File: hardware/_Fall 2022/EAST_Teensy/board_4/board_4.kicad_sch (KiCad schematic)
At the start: 7 parts, among them J1 Conn_01x04, J2 Conn_02x09_Odd_Even, U1 Teensy4.1

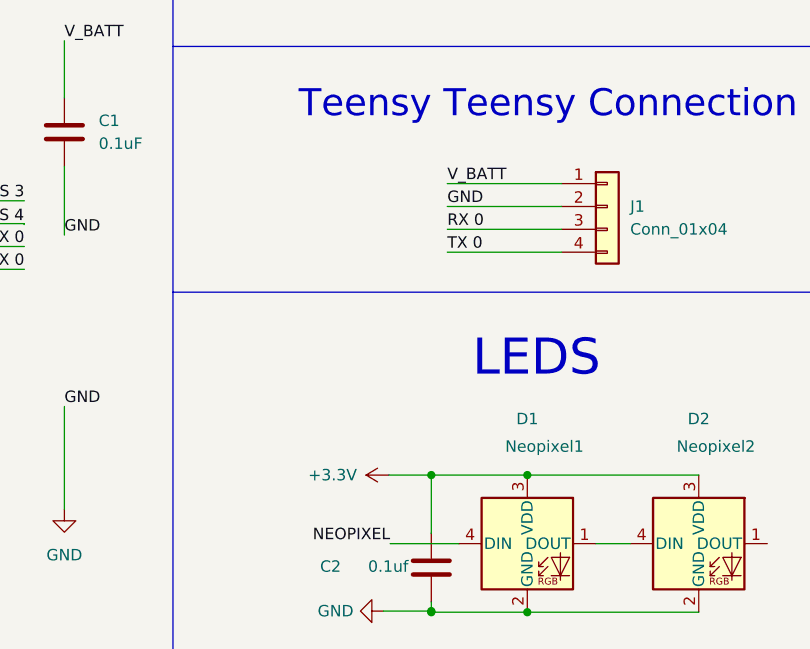
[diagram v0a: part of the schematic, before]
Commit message: Add final traces
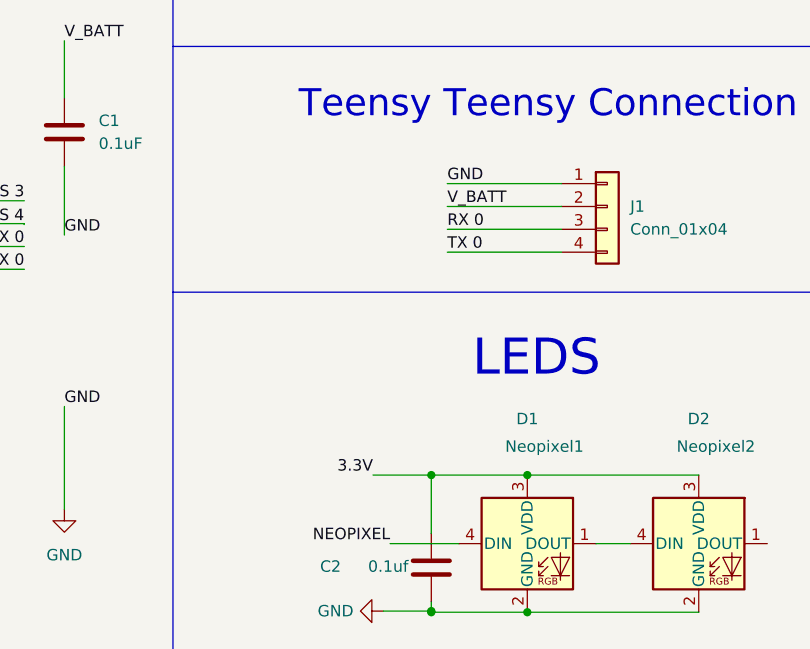
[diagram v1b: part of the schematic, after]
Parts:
- C1: JLC (none) -> C307380
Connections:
- net +3.3V is gone; now on net 3.3V: C2.2, D1.3 (VDD), D2.3 (VDD)
- net GND: now also J1.1 (Pin_1); no longer J1.2 (Pin_2)
- net V_BATT: now also J1.2 (Pin_2); no longer J1.1 (Pin_1)
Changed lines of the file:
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@@
     (stroke (width 0) (type default) (color 0 0 0 0))
   )
-  (wire (pts (xy 145.288 107.95) (xy 149.987 107.95))
+  (wire (pts (xy 143.51 107.95) (xy 149.987 107.95))
     (stroke (width 0) (type default) (color 0 0 0 0))
   )
@@
     (effects (font (size 1.27 1.27)) (justify left bottom))
   )
-  (label "GND" (at 151.765 78.105 0)
+  (label "V_BATT" (at 151.765 78.105 0)
     (effects (font (size 1.27 1.27)) (justify left bottom))
   )
@@
     (effects (font (size 1.27 1.27)) (justify left bottom))
   )
+  (label "3.3V" (at 143.51 107.95 180)
+    (effects (font (size 1.27 1.27)) (justify right bottom))
+  )
   (label "V_BATT" (at 109.22 59.69 0)
     (effects (font (size 1.27 1.27)) (justify left bottom))
   )
-  (label "V_BATT" (at 151.765 75.565 0)
+  (label "GND" (at 151.765 75.565 0)
     (effects (font (size 1.27 1.27)) (justify left bottom))
   )
@@
     )
     (property "Datasheet" "~" (id 3) (at 109.22 69.85 0)
+      (effects (font (size 1.27 1.27)) hide)
+    )
+    (property "JLC" "C307380" (id 4) (at 109.22 69.85 0)
       (effects (font (size 1.27 1.27)) hide)
     )
@@
     (pin "1")
   )
-  (symbol (lib_id "power:+3.3V") (at 145.288 107.95 90) (unit 1)
-    (in_bom yes) (on_board yes) (fields_autoplaced)
-    (property "Reference" "#PWR02" (id 0) (at 149.098 107.95 0)
-      (effects (font (size 1.27 1.27)) hide)
-    )
-    (property "Value" "+3.3V" (id 1) (at 141.732 107.9499 90)
-      (effects (font (size 1.27 1.27)) (justify left))
-    )
-    (property "Footprint" "" (id 2) (at 145.288 107.95 0)
-      (effects (font (size 1.27 1.27)) hide)
-    )
-    (property "Datasheet" "" (id 3) (at 145.288 107.95 0)
-      (effects (font (size 1.27 1.27)) hide)
-    )
-    (pin "1")
-  )
   (symbol (lib_id "Connector_Generic:Conn_01x04") (at 169.545 78.105 0) (unit 1)
     (in_bom yes) (on_board yes) (fields_autoplaced)
@@
       (reference "#PWR01") (unit 1) (value "GND") (footprint "")
     )
-    (path "/e1d09543-69b7-4602-aa24-2de0e8438245"
-      (reference "#PWR02") (unit 1) (value "+3.3V") (footprint "")
-    )
     (path "/a6798941-d529-4e1c-8239-a5393dc9268b"

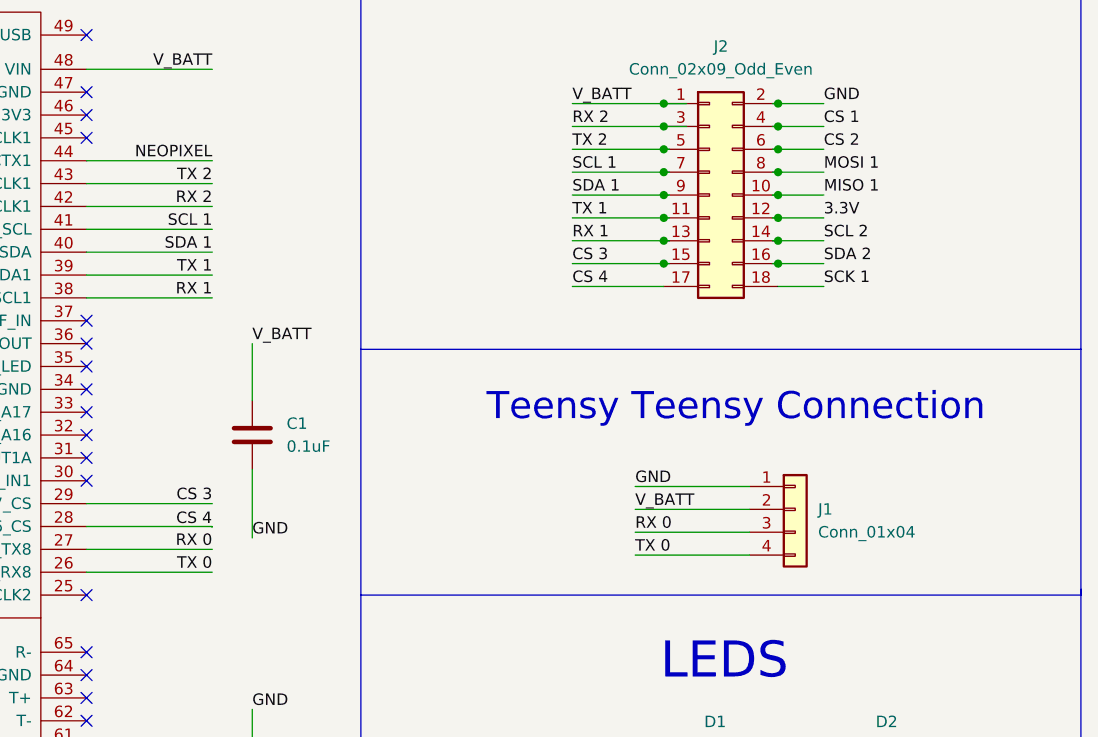
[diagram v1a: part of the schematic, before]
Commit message: Fix errors on TX/RX and added buzzer
Current state: Board 1 - need to check diodes; Board 4 - done; GPS- not showing layout traces, all need logos
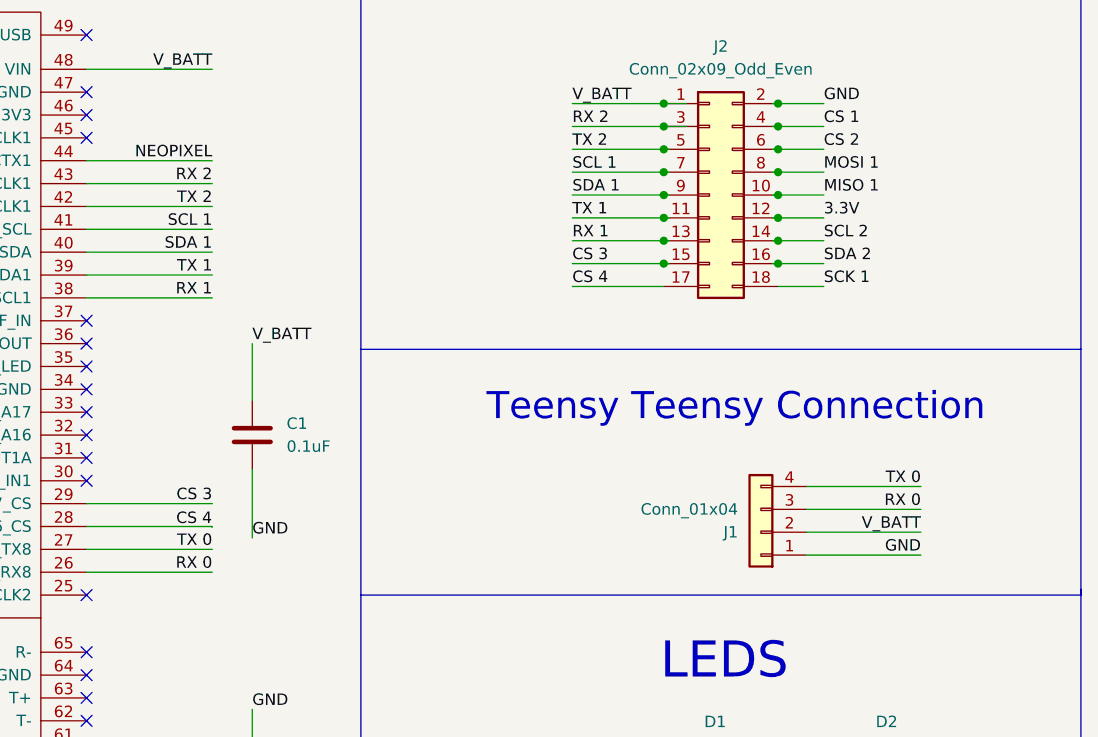
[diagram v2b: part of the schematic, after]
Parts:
- C2: JLC (none) -> C307380
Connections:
- net RX 0: now also U1.26 (34_RX8); no longer U1.27 (35_TX8)
- net RX 2: now also U1.43 (21_A7_RX5_BCLK1); no longer U1.42 (20_A6_TX5_LRCLK1)
- net TX 0: now also U1.27 (35_TX8); no longer U1.26 (34_RX8)
- net TX 2: now also U1.42 (20_A6_TX5_LRCLK1); no longer U1.43 (21_A7_RX5_BCLK1)
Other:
- moved on the sheet: J1
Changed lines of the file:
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@@
     (stroke (width 0) (type default) (color 0 0 0 0))
   )
-  (wire (pts (xy 151.765 75.565) (xy 164.465 75.565))
+  (wire (pts (xy 183.515 83.185) (xy 170.815 83.185))
     (stroke (width 0) (type default) (color 0 0 0 0))
   )
@@
     (stroke (width 0) (type default) (color 0 0 0 0))
   )
-  (wire (pts (xy 151.765 78.105) (xy 164.465 78.105))
+  (wire (pts (xy 183.515 80.645) (xy 170.815 80.645))
     (stroke (width 0) (type default) (color 0 0 0 0))
   )
@@
     (stroke (width 0) (type default) (color 0 0 0 0))
   )
-  (wire (pts (xy 151.765 83.185) (xy 164.465 83.185))
+  (wire (pts (xy 183.515 75.565) (xy 170.815 75.565))
     (stroke (width 0) (type default) (color 0 0 0 0))
   )
@@
     (stroke (width 0) (type default) (color 0 0 0 0))
   )
-  (wire (pts (xy 151.765 80.645) (xy 164.465 80.645))
+  (wire (pts (xy 183.515 78.105) (xy 170.815 78.105))
     (stroke (width 0) (type default) (color 0 0 0 0))
   )
@@
     (effects (font (size 1.27 1.27)) (justify left bottom))
   )
-  (label "RX 2" (at 104.775 44.45 180)
+  (label "TX 2" (at 104.775 44.45 180)
     (effects (font (size 1.27 1.27)) (justify right bottom))
   )
@@
     (effects (font (size 1.27 1.27)) (justify left bottom))
   )
-  (label "TX 2" (at 104.775 41.91 180)
-    (effects (font (size 1.27 1.27)) (justify right bottom))
-  )
-  (label "RX 0" (at 151.765 80.645 0)
-    (effects (font (size 1.27 1.27)) (justify left bottom))
+  (label "RX 2" (at 104.775 41.91 180)
+    (effects (font (size 1.27 1.27)) (justify right bottom))
+  )
+  (label "RX 0" (at 183.515 78.105 180)
+    (effects (font (size 1.27 1.27)) (justify right bottom))
   )
   (label "NEOPIXEL" (at 104.775 39.37 180)
@@
     (effects (font (size 1.27 1.27)) (justify left bottom))
   )
-  (label "V_BATT" (at 151.765 78.105 0)
-    (effects (font (size 1.27 1.27)) (justify left bottom))
+  (label "V_BATT" (at 183.515 80.645 180)
+    (effects (font (size 1.27 1.27)) (justify right bottom))
   )
   (label "SDA 1" (at 104.775 49.53 180)
@@
     (effects (font (size 1.27 1.27)) (justify left bottom))
   )
-  (label "GND" (at 151.765 75.565 0)
-    (effects (font (size 1.27 1.27)) (justify left bottom))
+  (label "GND" (at 183.515 83.185 180)
+    (effects (font (size 1.27 1.27)) (justify right bottom))
   )
   (label "CS 2" (at 172.72 38.1 0)
@@
     (effects (font (size 1.27 1.27)) (justify left bottom))
   )
-  (label "TX 0" (at 104.775 85.09 180)
+  (label "RX 0" (at 104.775 85.09 180)
     (effects (font (size 1.27 1.27)) (justify right bottom))
   )
@@
     (effects (font (size 1.27 1.27)) (justify left bottom))
   )
-  (label "RX 0" (at 104.775 82.55 180)
+  (label "TX 0" (at 104.775 82.55 180)
     (effects (font (size 1.27 1.27)) (justify right bottom))
   )
@@
     (effects (font (size 1.27 1.27)) (justify left bottom))
   )
-  (label "TX 0" (at 151.765 83.185 0)
-    (effects (font (size 1.27 1.27)) (justify left bottom))
+  (label "TX 0" (at 183.515 75.565 180)
+    (effects (font (size 1.27 1.27)) (justify right bottom))
   )
   (symbol (lib_id "Connector_Generic:Conn_02x09_Odd_Even") (at 160.02 43.18 0) (unit 1)
@@
     )
     (property "Datasheet" "~" (id 3) (at 149.987 118.237 0)
+      (effects (font (size 1.27 1.27)) hide)
+    )
+    (property "JLC" "C307380" (id 4) (at 149.987 118.237 0)
       (effects (font (size 1.27 1.27)) hide)
     )
@@
     (pin "1")
   )
-  (symbol (lib_id "Connector_Generic:Conn_01x04") (at 169.545 78.105 0) (unit 1)
+  (symbol (lib_id "Connector_Generic:Conn_01x04") (at 165.735 80.645 180) (unit 1)
     (in_bom yes) (on_board yes) (fields_autoplaced)
-    (property "Reference" "J1" (id 0) (at 172.085 78.1049 0)
+    (property "Reference" "J1" (id 0) (at 163.195 80.6451 0)
       (effects (font (size 1.27 1.27)) (justify left))
     )
-    (property "Value" "Conn_01x04" (id 1) (at 172.085 80.6449 0)
+    (property "Value" "Conn_01x04" (id 1) (at 163.195 78.1051 0)
       (effects (font (size 1.27 1.27)) (justify left))
     )
-    (property "Footprint" "Connector_JST:JST_PH_S4B-PH-K_1x04_P2.00mm_Horizontal" (id 2) (at 169.545 78.105 0)
-      (effects (font (size 1.27 1.27)) hide)
-    )
-    (property "Datasheet" "~" (id 3) (at 169.545 78.105 0)
-      (effects (font (size 1.27 1.27)) hide)
-    )
+    (property "Footprint" "Connector_JST:JST_PH_S4B-PH-K_1x04_P2.00mm_Horizontal" (id 2) (at 165.735 80.645 0)
+      (effects (font (size 1.27 1.27)) hide)
+    )
+    (property "Datasheet" "~" (id 3) (at 165.735 80.645 0)
+      (effects (font (size 1.27 1.27)) hide)
+    )

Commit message: change board 4 C size and GPS labels hided
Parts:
- C1: footprint Capacitor_SMD:C_0201_0603Metric -> Capacitor_SMD:C_0603_1608Metric
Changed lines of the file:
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@@
       (effects (font (size 1.27 1.27)) (justify left))
     )
-    (property "Footprint" "Capacitor_SMD:C_0201_0603Metric" (id 2) (at 110.1852 73.66 0)
+    (property "Footprint" "Capacitor_SMD:C_0603_1608Metric" (id 2) (at 110.1852 73.66 0)
       (effects (font (size 1.27 1.27)) hide)
     )
@@
     )
     (path "/82e280a4-56a4-4b9c-912d-48b78e5c2f29"
-      (reference "C1") (unit 1) (value "0.1uF") (footprint "Capacitor_SMD:C_0201_0603Metric")
+      (reference "C1") (unit 1) (value "0.1uF") (footprint "Capacitor_SMD:C_0603_1608Metric")
     )
     (path "/509c503b-65f7-47ea-a38c-398e1359983b"

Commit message: minor fixes
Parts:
- C1: JLC C307380 -> (none); Vendor (none) -> C14663
- C2: footprint Capacitor_SMD:C_0201_0603Metric -> Capacitor_SMD:C_0603_1608Metric; JLC C307380 -> (none); Vendor (none) -> C14663
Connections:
- net GND: now also J1.4 (Pin_4); no longer J1.1 (Pin_1)
- net RX 0: now also J1.2 (Pin_2); no longer J1.3 (Pin_3)
- net TX 0: now also J1.1 (Pin_1); no longer J1.4 (Pin_4)
- net V_BATT: now also J1.3 (Pin_3); no longer J1.2 (Pin_2)
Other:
- moved on the sheet: J1
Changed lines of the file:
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@@
     (stroke (width 0) (type default) (color 0 0 0 0))
   )
-  (wire (pts (xy 183.515 83.185) (xy 170.815 83.185))
+  (wire (pts (xy 182.118 83.312) (xy 169.418 83.312))
     (stroke (width 0) (type default) (color 0 0 0 0))
   )
@@
     (stroke (width 0) (type default) (color 0 0 0 0))
   )
-  (wire (pts (xy 183.515 80.645) (xy 170.815 80.645))
+  (wire (pts (xy 182.118 80.772) (xy 169.418 80.772))
     (stroke (width 0) (type default) (color 0 0 0 0))
   )
@@
     (stroke (width 0) (type default) (color 0 0 0 0))
   )
-  (wire (pts (xy 183.515 75.565) (xy 170.815 75.565))
+  (wire (pts (xy 182.118 75.692) (xy 169.418 75.692))
     (stroke (width 0) (type default) (color 0 0 0 0))
   )
@@
     (stroke (width 0) (type default) (color 0 0 0 0))
   )
-  (wire (pts (xy 183.515 78.105) (xy 170.815 78.105))
+  (wire (pts (xy 182.118 78.232) (xy 169.418 78.232))
     (stroke (width 0) (type default) (color 0 0 0 0))
   )
@@
     (effects (font (size 1.27 1.27)) (justify right bottom))
   )
-  (label "RX 0" (at 183.515 78.105 180)
+  (label "RX 0" (at 182.118 78.232 180)
     (effects (font (size 1.27 1.27)) (justify right bottom))
   )
@@
     (effects (font (size 1.27 1.27)) (justify left bottom))
   )
-  (label "V_BATT" (at 183.515 80.645 180)
+  (label "V_BATT" (at 182.118 80.772 180)
     (effects (font (size 1.27 1.27)) (justify right bottom))
   )
@@
     (effects (font (size 1.27 1.27)) (justify left bottom))
   )
-  (label "GND" (at 183.515 83.185 180)
+  (label "GND" (at 182.118 83.312 180)
     (effects (font (size 1.27 1.27)) (justify right bottom))
   )
@@
     (effects (font (size 1.27 1.27)) (justify left bottom))
   )
-  (label "TX 0" (at 183.515 75.565 180)
+  (label "TX 0" (at 182.118 75.692 180)
     (effects (font (size 1.27 1.27)) (justify right bottom))
   )
@@
       (effects (font (size 1.27 1.27)) (justify left))
     )
-    (property "Footprint" "Capacitor_SMD:C_0201_0603Metric" (id 2) (at 149.0218 114.427 0)
+    (property "Footprint" "Capacitor_SMD:C_0603_1608Metric" (id 2) (at 149.0218 114.427 0)
       (effects (font (size 1.27 1.27)) hide)
     )
@@
       (effects (font (size 1.27 1.27)) hide)
     )
-    (property "JLC" "C307380" (id 4) (at 149.987 118.237 0)
+    (property "Vendor" "C14663" (id 4) (at 149.987 118.237 0)
       (effects (font (size 1.27 1.27)) hide)
     )
@@
       (effects (font (size 1.27 1.27)) hide)
     )
-    (property "JLC" "C307380" (id 4) (at 109.22 69.85 0)
+    (property "Vendor" "C14663" (id 4) (at 109.22 69.85 0)
       (effects (font (size 1.27 1.27)) hide)
     )
@@
     (pin "1")
   )
-  (symbol (lib_id "Connector_Generic:Conn_01x04") (at 165.735 80.645 180) (unit 1)
+  (symbol (lib_id "Connector_Generic:Conn_01x04") (at 164.338 78.232 0) (mirror y) (unit 1)
     (in_bom yes) (on_board yes) (fields_autoplaced)
-    (property "Reference" "J1" (id 0) (at 163.195 80.6451 0)
-      (effects (font (size 1.27 1.27)) (justify left))
-    )
-    (property "Value" "Conn_01x04" (id 1) (at 163.195 78.1051 0)
-      (effects (font (size 1.27 1.27)) (justify left))
-    )
-    (property "Footprint" "Connector_JST:JST_PH_S4B-PH-K_1x04_P2.00mm_Horizontal" (id 2) (at 165.735 80.645 0)
-      (effects (font (size 1.27 1.27)) hide)
-    )
-    (property "Datasheet" "~" (id 3) (at 165.735 80.645 0)
+    (property "Reference" "J1" (id 0) (at 164.338 68.707 0))
+    (property "Value" "Conn_01x04" (id 1) (at 164.338 71.247 0))
+    (property "Footprint" "Connector_JST:JST_PH_S4B-PH-K_1x04_P2.00mm_Horizontal" (id 2) (at 164.338 78.232 0)
+      (effects (font (size 1.27 1.27)) hide)
+    )
+    (property "Datasheet" "~" (id 3) (at 164.338 78.232 0)
       (effects (font (size 1.27 1.27)) hide)
     )
@@
     )
     (path "/509c503b-65f7-47ea-a38c-398e1359983b"
-      (reference "C2") (unit 1) (value "0.1uf") (footprint "Capacitor_SMD:C_0201_0603Metric")
+      (reference "C2") (unit 1) (value "0.1uf") (footprint "Capacitor_SMD:C_0603_1608Metric")
     )
     (path "/b88239bc-ae48-46ce-a575-bdfc495bad18"

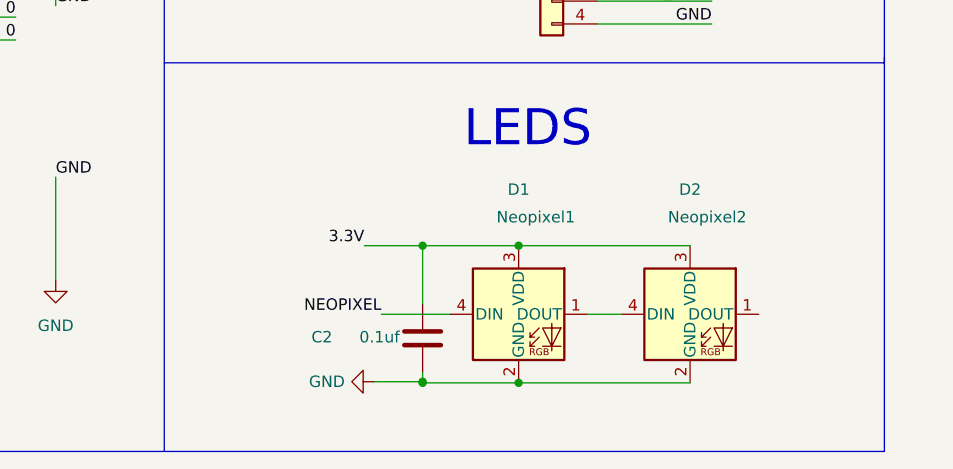
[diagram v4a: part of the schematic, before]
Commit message: Changed neopixel on board 4
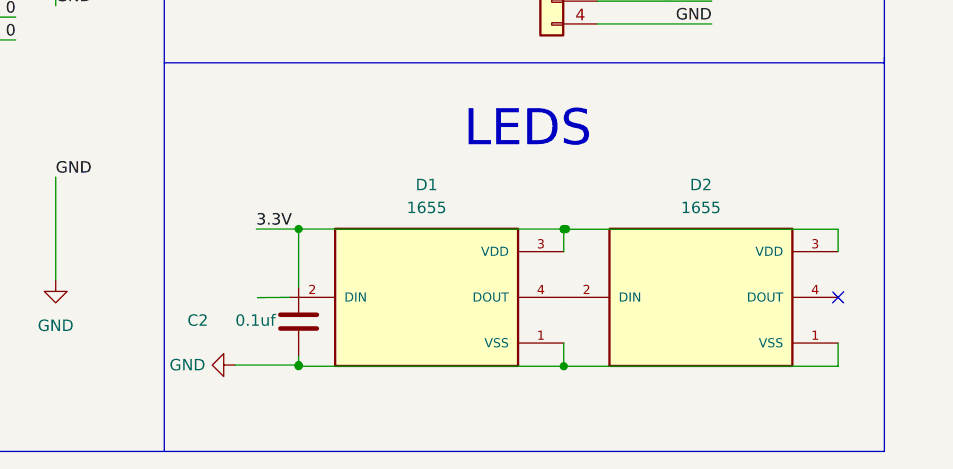
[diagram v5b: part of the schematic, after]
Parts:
- removed D1: Neopixel1, Neopixel:LED_1655, symbol LED:NeoPixel_THT
- removed D2: Neopixel2, Neopixel:LED_1655, symbol LED:NeoPixel_THT
- added D1, D2: 1655, LED_1655, symbol neopixel:1655
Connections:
- net 3.3V: now also D1.3 (VDD), D2.3 (VDD)
- net GND: now also D1.1 (VSS), D2.1 (VSS)
- new net: D1.4 (DOUT), D2.2 (DIN)
- no-connect marks 46 -> 47

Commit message: pcb fixes
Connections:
- net NEOPIXEL: now also D1.2 (DIN)
- net SCK: now reaches U1.35 (13_SCK_LED)
- net SCK: now also J2.18 (Pin_18)
- net MISO 1 renamed MISO
- net MOSI 1 renamed MOSI
- net RX 0 renamed RX 8
- net RX 1 renamed RX 4
- net RX 2 renamed RX 5
- net SCK 1: no longer names the net of U1.19 (27_A13_SCK1)
- net SCK 1: no longer J2.18 (Pin_18)
- net TX 0 renamed TX 8
- net TX 1 renamed TX 4
- net TX 2 renamed TX 5
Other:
- moved on the sheet: C2, D1, D2
